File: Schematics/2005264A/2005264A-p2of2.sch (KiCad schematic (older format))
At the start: 65 parts, among them J3 ConnectorA1-300, J4 ConnectorA1-400, U202 D3NOR-+4SW-0VDCA-ABC-_F_, U203 D3NOR-FAP-0VDCA-expander-ABC-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, U204 D3NOR-+4SW-0VDCA-_C_-E_F, U205 D3NOR-+4SW-0VDCA-B_C-_F_, U206 D3NOR-+4SW-0VDCA-B_C-E_F, U207 D3NOR-+4SW-0VDCA-ABC-_F_, U208 D3NOR-FAP-0VDCA-expander-ABC-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, U209 D3NOR-+4SW-0VDCA-B_C-_F_, U210 D3NOR-+4SW-0VDCA-_C_-_F_, U211 D3NOR-+4SW-0VDCA-ABC-_F_, U212 D3NOR-FAP-0VDCA-expander-ABC-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, U213 D3NOR-+4SW-0VDCA-ACB-_F_, U214 D3NOR-+4SW-0VDCA-_C_-_F_, U215 D3NOR-+4SW-0VDCA-_C_-DEF, U216 D3NOR-FAP-0VDCA-expander-ABC-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, U217 D3NOR-+4SW-0VDCA-_C_-_F_, U218 D3NOR-+4SW-0VDCA-ACB-_F_, U219 D3NOR-+4SW-0VDCA-_C_-_F_, U220 D3NOR-+4SW-0VDCA-ABC-_F_, U221 D3NOR-+4SW-0VDCA-_C_-_F_, U222 D3NOR-FAP-0VDCA-expander-ABC-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, U223 D3NOR-+4SW-0VDCA-BAC-_F_, U224 D3NOR-+4SW-0VDCA-_C_-_F_, U225 D3NOR-+4SW-0VDCA-BAC-_F_, U226 D3NOR-+4SW-0VDCA-_C_-_F_, U227 D3NOR-FAP-0VDCA-expander-ABC-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, U228 D3NOR-+4SW-0VDCA-_C_-DEF, U229 D3NOR-+4SW-0VDCA-_C_-_F_, U230 D3NOR-+4SW-0VDCA-_C_-DEF, U231 D3NOR-+4SW-0VDCA-B_C-E_F, U232 D3NOR-+4SW-0VDCA-_C_-E_F, U233 D3NOR-+4SW-0VDCA-_C_-_F_, U234 D3NOR-+4SW-0VDCA-BAC-_F_, U235 D3NOR-+4SW-0VDCA-_C_-_F_, U236 D3NOR-+4SW-0VDCA-_C_-DFE, U237 D3NOR-+4SW-0VDCA-_C_-E_F, U238 D3NOR-FAP-0VDCA-expander-ABC-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, U239 D3NOR-FAP-0VDCA-expander-B_C-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, U240 D3NOR-+4SW-0VDCA-_C_-_F_, U241 D3NOR-+4SW-0VDCA-B_C-DFE, U242 D3NOR-+4SW-0VDCA-ACB-DFE, U243 D3NOR-FAP-0VDCA-expander-B_C-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, U244 D3NOR-+4SW-0VDCA-ABC-E_F, U245 D3NOR-+4SW-0VDCA-_C_-_F_, U246 D3NOR-FAP-0VDCA-expander-ABC-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, U247 D3NOR-+4SW-0VDCA-_C_-DFE, U248 D3NOR-+4SW-0VDCA-_C_-EDF, U249 D3NOR-FAP-0VDCA-expander-ABC-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, U250 D3NOR-+4SW-0VDCA-_C_-_F_, U251 D3NOR-+4SW-0VDCA-_C_-EDF, U252 D3NOR-+4SW-0VDCA-ACB-_F_, U253 D3NOR-+4SW-0VDCA-_C_-_F_, U254 D3NOR-FAP-0VDCA-expander-ABC-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, U255 D3NOR-+4SW-0VDCA-_C_-DEF, U256 D3NOR-+4SW-0VDCA-_C_-EDF, U257 D3NOR-+4SW-0VDCA-_C_-_F_, U258 D3NOR-FAP-0VDCA-expander-ABC-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, U259 D3NOR-+4SW-0VDCA-ACB-_F_, U260 D3NOR-+4SW-0VDCA-_C_-DFE, X1 ArrowTwiddle, X2 ArrowTwiddle, X3 ArrowTwiddle

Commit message: Added CAD files for drawing 2005264A.  Made several corrections to 2005264B that I found during the process.
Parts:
- J4: Caption 0VDCA -> WT/
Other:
- note added: "Notes from the Virtual AGC Project:\n1. This CAD drawing was adapted from the previously-transcribed original Apollo\n Program drawing 2005264B and checked vs the original drawing 2005264A (and\n 2005064F). It does not itself date from the Apollo period. — RSB 2018\n2. The original drawing displayed no reference designators for the components, so\n this CAD drawing also does not display any. For 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"
- note removed: "B REVISED PER TDRR 35326"
- note removed: "Notes from the Virtual AGC Project:\n1. This CAD drawing was manually transcribed from the original Apollo Program \n drawing 2005264B, but does not itself date from the Apollo period. — RSB 2018\n2. The original drawing displayed no reference designators for the components, so\n this CAD drawing also does not display any. For the purposes of ERC or netlist\n generation, NOR gates have reference 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"
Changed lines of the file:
@@
 Text Notes 38875 33400 0    140  ~ 28
 ____
-Wire Notes Line width 6 style solid
-	43500 1300 36461 1300
-Text Notes 36550 1250 0    160  ~ 32
-A      REVISED PER TDRR 30754
-Wire Notes Line width 6 style solid
-	43500 1625 36461 1625
-Wire Notes Line width 6 style solid
-	36461 975  36461 1625
-Wire Notes Line width 6 style solid
-	36839 975  36839 1625
-Wire Notes Line width 6 style solid
-	37350 975  37350 1625
-Wire Notes Line width 6 style solid
-	40831 975  40831 1625
-Wire Notes Line width 6 style solid
-	41331 975  41331 1625
-Wire Notes Line width 6 style solid
-	41831 975  41831 1625
-Wire Notes Line width 6 style solid
-	42480 975  42480 1625
-Text Notes 36525 1575 0    160  ~ 32
-B      REVISED PER TDRR 35326
 Text Notes 42425 33450 0    140  ~ 28
 2     2
@@
 F 2 "" H 24725 5300 140 0001 C CNN
 F 3 "" H 24725 5300 140 0001 C CNN
-F 4 "0VDCA" H 24550 5150 140 0000 C CNB "Caption"
+F 4 "WT/" H 24675 5175 140 0000 C CNB "Caption"
 	17   24725 4825
 	1    0    0    -1
@@
 F 2 "" H 9975 16175 140 0001 C CNN
 F 3 "" H 9975 16175 140 0001 C CNN
-F 4 "XB4/" H 9950 15375 140 0000 C CNB "Caption"
+F 4 "XB4/" H 9925 15375 140 0000 C CNB "Caption"
 	39   9975 15700
 	-1   0    0    1
@@
 $EndComp
 Text Notes 1175 33275 0    140  ~ 28
-Notes from the Virtual AGC Project:\n1. This CAD drawing was manually transcribed from the original Apollo Program \n   drawing 2005264B, but does not itself date from the Apollo period. — RSB 2018\n2. The original drawing displayed no reference designators for the components, so\n   this CAD drawing also does not display any.  For the purposes of ERC or netlist\n   generation, NOR gates have reference designators U2nn, where nn is the 2-digit\n   number shown on the NOR-gate symbol.  The oval pads numbered 301-371\n   comprise connector J3, while those numbered 401-471 comprise connector J4.\n   — RSB 2018\n3. All known revisions of this drawing incorrectly display the 2-digit location code of\n   NOR gate 42416 as "K".  On this CAD drawing, we have used location code "54",\n   so that the gate forms U254 (along with NOR gate 42412). — RSB 2018\n4. The originals of sheets 1 and 2 of drawing 2005264B used different \n   area-numbering systems.  Sheet 1 used border numbers 1-6 and border letters A-F,\n   while sheet 2 used numbers 1-8 and letters A-H.  The CAD schematic editor being\n   used does not provide the option of doing this, so the CAD drawing instead uses the\n   area-numbering system from sheet 1 for both sheets.\n5. The only change I have been able to find from drawing 2005264A to 2005264B is\n   that the caption of oval pad 417 has changed from "WT/" to "0VDCA". — RSB 2018
+Notes from the Virtual AGC Project:\n1. This CAD drawing was adapted from the previously-transcribed original Apollo\n   Program drawing 2005264B and checked vs the original drawing 2005264A (and\n   2005064F).  It does not itself date from the Apollo period.  — RSB 2018\n2. The original drawing displayed no reference designators for the components, so\n   this CAD drawing also does not display any.  For the purposes of ERC or netlist\n   generation, NOR gates have reference designators U2nn, where nn is the 2-digit\n   number shown on the NOR-gate symbol.  The oval pads numbered 301-371\n   comprise connector J3, while those numbered 401-471 comprise connector J4.\n   — RSB 2018\n3. All known revisions of this drawing incorrectly display the 2-digit location code of\n   NOR gate 42416 as "K".  On this CAD drawing, we have used location code "54",\n   so that the gate forms U254 (along with NOR gate 42412). — RSB 2018\n4. The originals of sheets 1 and 2 of drawing 2005264A used different \n   area-numbering systems.  Sheet 1 used border numbers 1-6 and border letters A-F,\n   while sheet 2 used numbers 1-8 and letters A-H.  The CAD schematic editor being\n   used does not provide the option of doing this, so the CAD drawing instead uses the\n   area-numbering system from sheet 1 for both sheets.
 Wire Wire Line
 	8125 4525 8350 4525
@@
 Wire Wire Line
 	16725 16125 17000 16125
+Wire Notes Line width 6 style solid
+	43500 1300 36461 1300
+Text Notes 36550 1250 0    160  ~ 32
+A      REVISED PER TDRR 30754
+Wire Notes Line width 6 style solid
+	36461 975  36461 1300
+Wire Notes Line width 6 style solid
+	36839 975  36839 1300
+Wire Notes Line width 6 style solid
+	37350 975  37350 1300
+Wire Notes Line width 6 style solid
+	40831 975  40831 1300
+Wire Notes Line width 6 style solid
+	41331 975  41331 1300
+Wire Notes Line width 6 style solid
+	41831 975  41831 1300
+Wire Notes Line width 6 style solid
+	42480 975  42480 1300
 $Bitmap
-Pos 925  29000
+Pos 925  29225
 Scale 1.000000
 Data

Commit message: Finished up CAD for 2005264-, and made a correction to 2005264A & B based on the proofing for it.
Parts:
- J3: Caption XB73 -> XB7E
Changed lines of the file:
@@
 EESchema Schematic File Version 4
-LIBS:module-cache
 EELAYER 26 0
 EELAYER END
 $Descr E 44000 34000
 encoding utf-8
-Sheet 3 3
+Sheet 1 1
 Title ""
 Date ""
@@
 F 2 "" H 11425 27300 140 0001 C CNN
 F 3 "" H 11425 27300 140 0001 C CNN
-F 4 "XB73" H 11450 26475 140 0000 C CNB "Caption"
+F 4 "XB7E" H 11450 26475 140 0000 C CNB "Caption"
 	25   11425 26825
 	-1   0    0    1

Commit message: Cross-checked/corrected module A14's 2005264A and 2005264B drawings vs pin database.  Predecessor drawings (2005264- etc.) not yet corrected.
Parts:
- J3, J4: Caption (none) -> 0VDCA
- J3: Caption 208 -> S08
- J3, J4: Caption (none) -> +4SW
- J4: Caption WSC6/ -> WSCG/
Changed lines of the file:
@@
 EESchema Schematic File Version 4
+LIBS:module-cache
 EELAYER 26 0
 EELAYER END
 $Descr E 44000 34000
 encoding utf-8
-Sheet 1 1
+Sheet 3 3
 Title ""
 Date ""
@@
 F 2 "" H 31650 5275 140 0001 C CNN
 F 3 "" H 31650 5275 140 0001 C CNN
-F 4 "WSC6/" H 31675 4450 140 0000 C CNB "Caption"
+F 4 "WSCG/" H 31675 4450 140 0000 C CNB "Caption"
 	11   31650 4800
 	-1   0    0    1
@@
 F 2 "" H 40350 27475 140 0001 C CNN
 F 3 "" H 40350 27475 140 0001 C CNN
-F 4 "" H 40350 27300 140 0000 C CNB "Caption"
+F 4 "0VDCA" H 40350 27300 140 0001 C CNB "Caption"
 	12   40350 27000
 	1    0    0    -1
@@
 F 2 "" H 36475 28500 140 0001 C CNN
 F 3 "" H 36475 28500 140 0001 C CNN
-F 4 "" H 36475 28325 140 0000 C CNB "Caption"
+F 4 "0VDCA" H 36475 28325 140 0001 C CNB "Caption"
 	60   36475 28025
 	1    0    0    -1
@@
 F 2 "" H 40350 28475 140 0001 C CNN
 F 3 "" H 40350 28475 140 0001 C CNN
-F 4 "" H 40350 28300 140 0000 C CNB "Caption"
+F 4 "0VDCA" H 40350 28300 140 0001 C CNB "Caption"
 	60   40350 28000
 	1    0    0    -1
@@
 F 2 "" H 40350 27975 140 0001 C CNN
 F 3 "" H 40350 27975 140 0001 C CNN
-F 4 "" H 40350 27800 140 0000 C CNB "Caption"
+F 4 "0VDCA" H 40350 27800 140 0001 C CNB "Caption"
 	36   40350 27500
 	1    0    0    -1
@@
 F 2 "" H 40350 29800 140 0001 C CNN
 F 3 "" H 40350 29800 140 0001 C CNN
-F 4 "" H 40350 29625 140 0000 C CNB "Caption"
+F 4 "+4SW" H 40350 29625 140 0001 C CNB "Caption"
 	48   40350 29325
 	1    0    0    -1
@@
 F 2 "" H 36475 29325 140 0001 C CNN
 F 3 "" H 36475 29325 140 0001 C CNN
-F 4 "" H 36475 29150 140 0000 C CNB "Caption"
+F 4 "+4SW" H 36475 29150 140 0001 C CNB "Caption"
 	24   36475 28850
 	1    0    0    -1
@@
 F 2 "" H 40325 29300 140 0001 C CNN
 F 3 "" H 40325 29300 140 0001 C CNN
-F 4 "" H 40325 29125 140 0000 C CNB "Caption"
+F 4 "+4SW" H 40325 29125 140 0001 C CNB "Caption"
 	24   40325 28825
 	1    0    0    -1
@@
 F 2 "" H 12175 6500 140 0001 C CNN
 F 3 "" H 12175 6500 140 0001 C CNN
-F 4 "208" H 12175 6325 140 0000 C CNB "Caption"
+F 4 "S08" H 12175 6325 140 0000 C CNB "Caption"
 	17   12175 6025
 	1    0    0    -1
@@
 F 2 "" H 36475 27500 140 0001 C CNN
 F 3 "" H 36475 27500 140 0001 C CNN
-F 4 "" H 36475 27325 140 0000 C CNB "Caption"
+F 4 "0VDCA" H 36475 27325 140 0001 C CNB "Caption"
 	12   36475 27025
 	1    0    0    -1

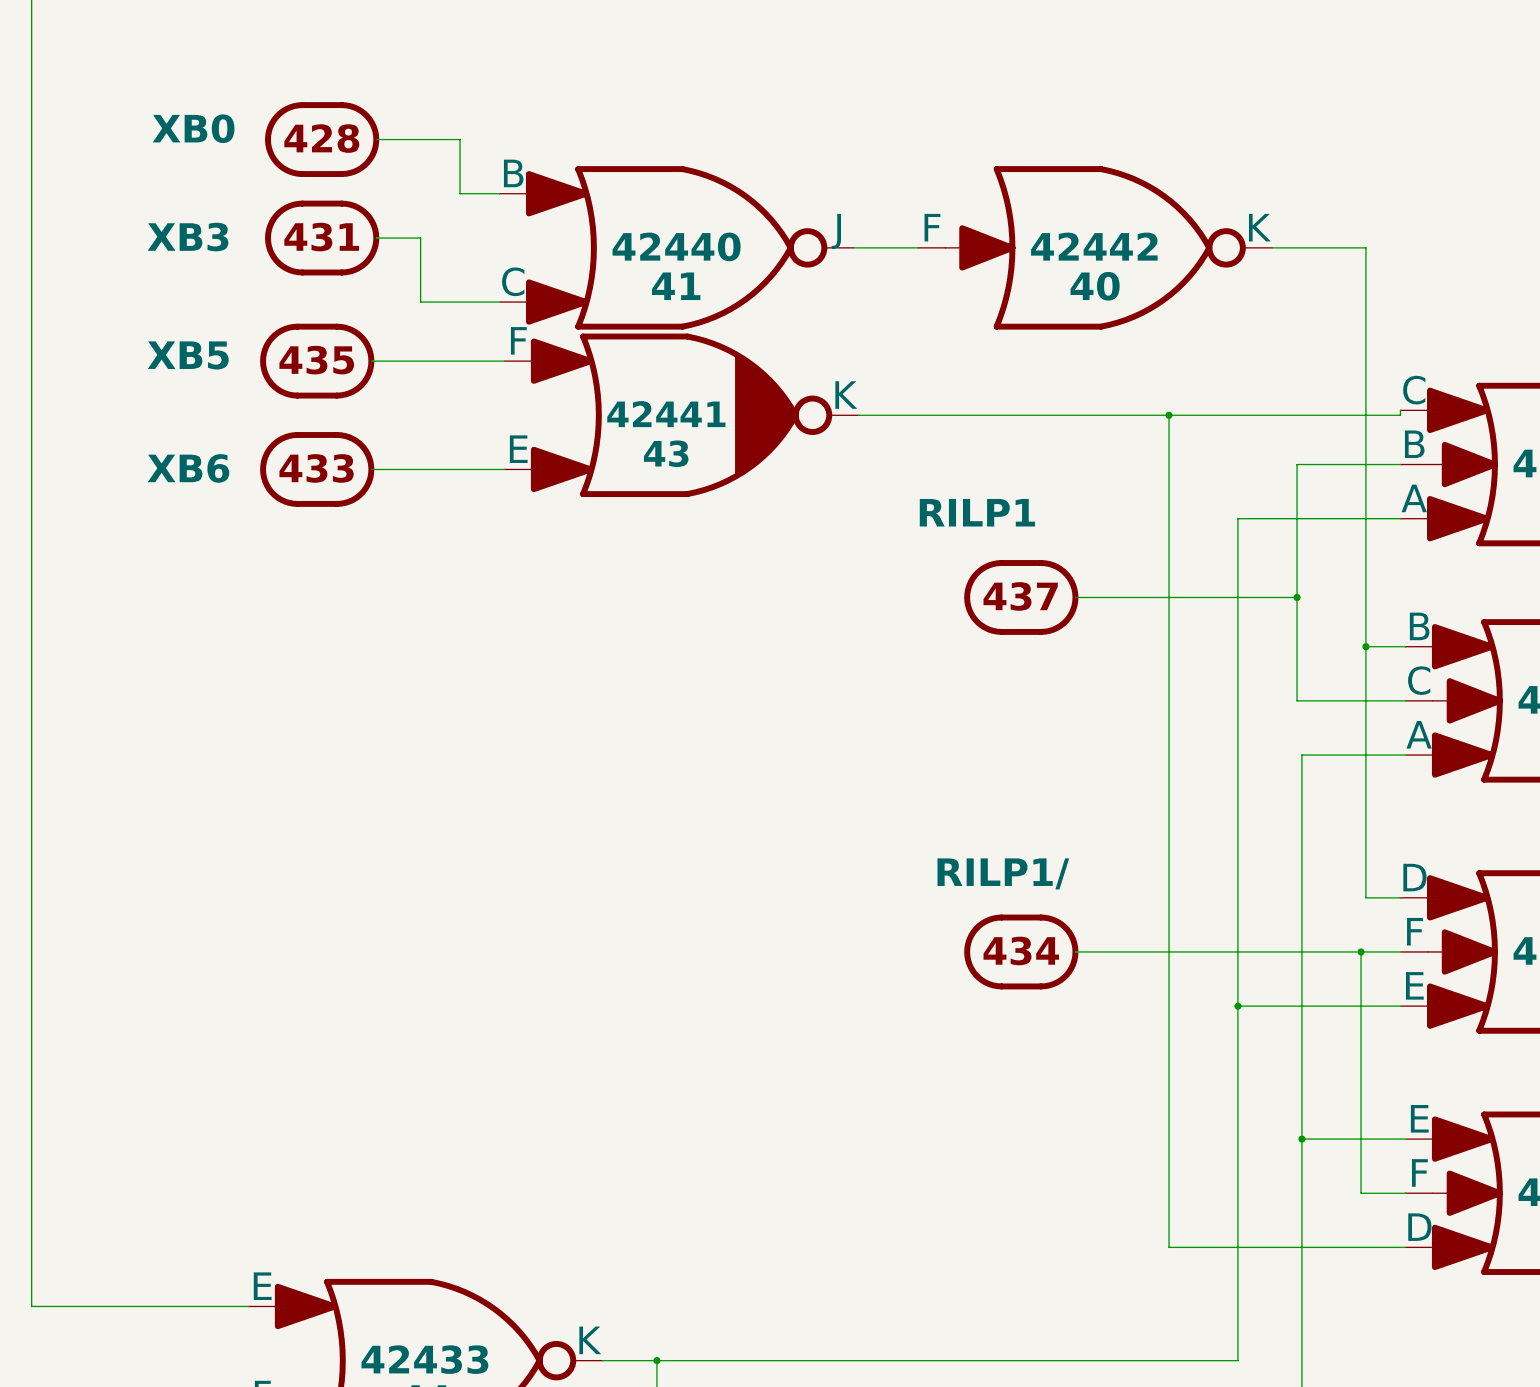
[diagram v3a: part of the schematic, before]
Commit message: Corrected a wiring bug.
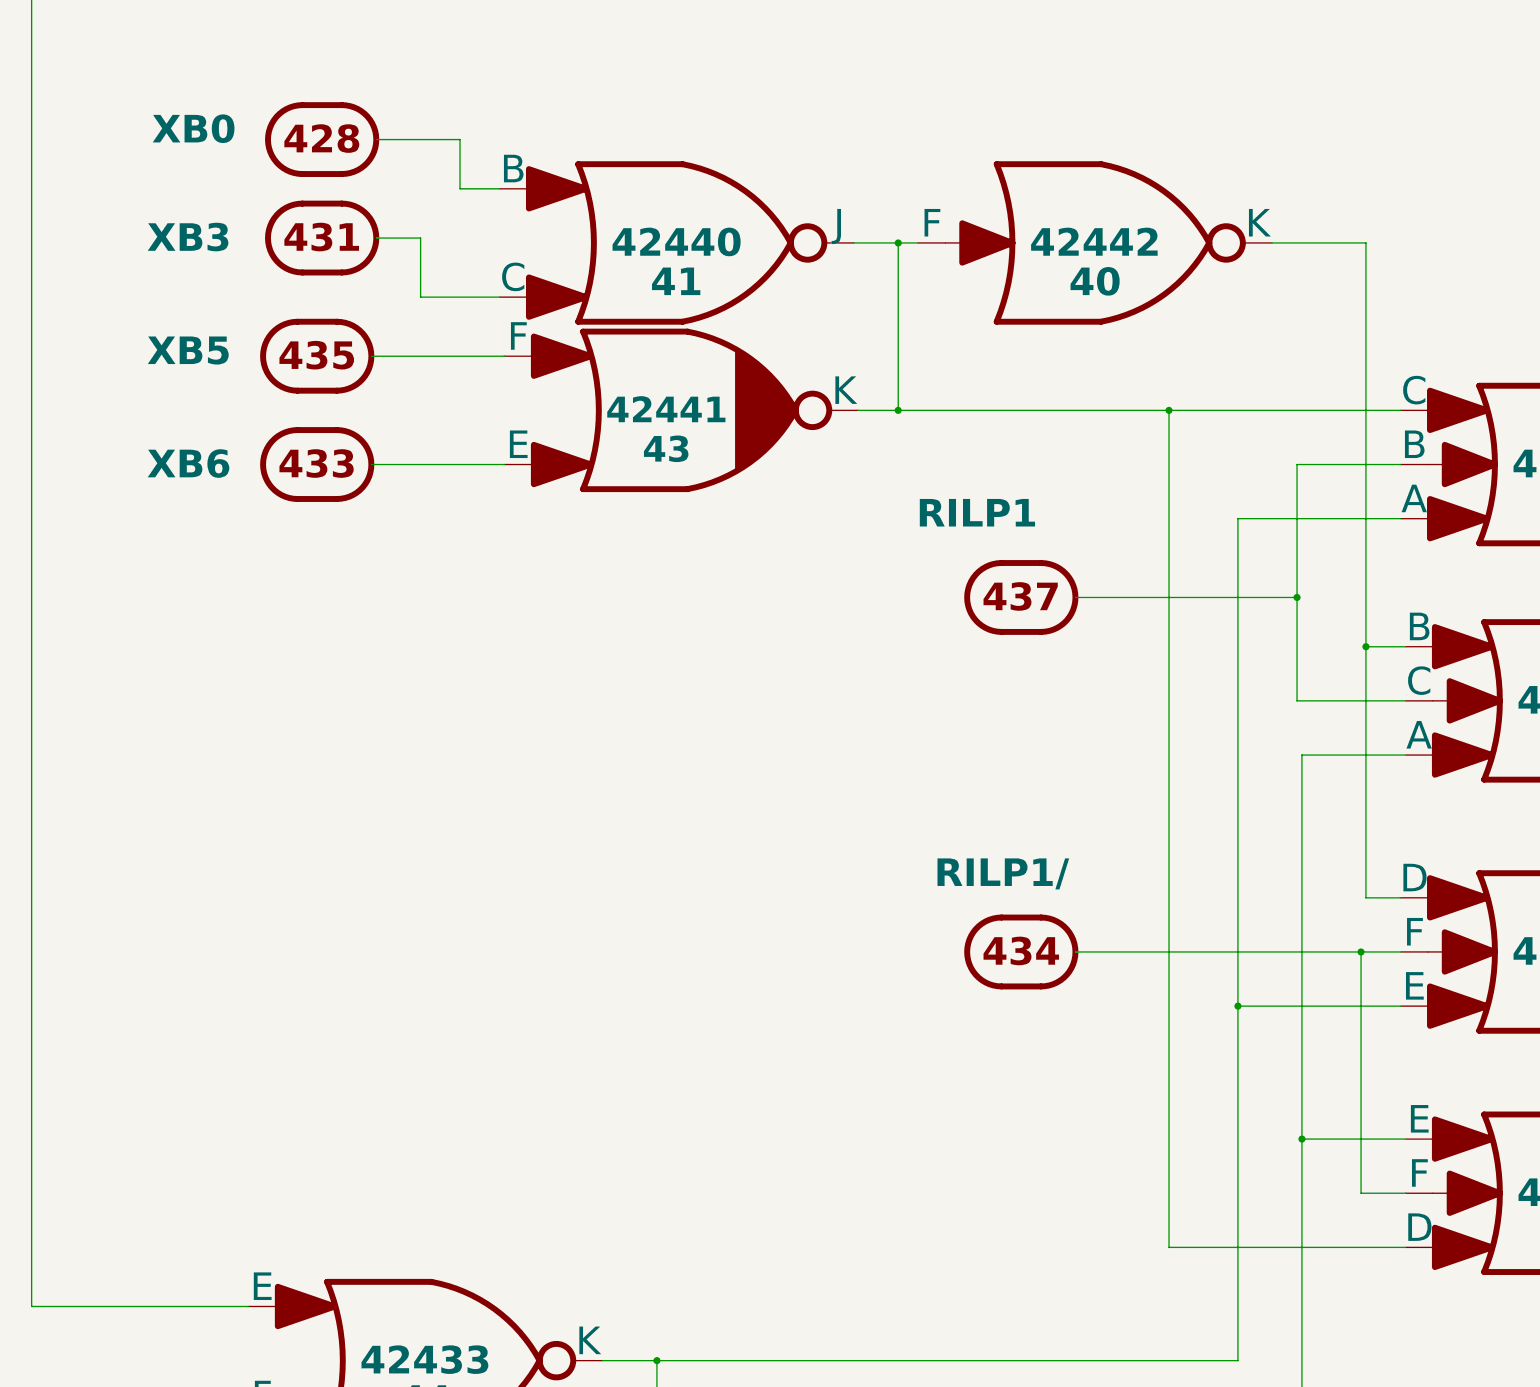
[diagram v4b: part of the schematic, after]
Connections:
- net at U241.6 (D), U243.9 (K), U244.2 (C): now also U240.8 (F), U241.1 (J)
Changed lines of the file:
@@
 EESchema Schematic File Version 4
 LIBS:module-cache
-EELAYER 26 0
+EELAYER 29 0
 EELAYER END
 $Descr E 44000 34000
@@
 L D3NOR-FAP-0VDCA-expander:D3NOR-FAP-0VDCA-expander-B_C-E_F U243
 U 2 1 5F3BC912
-P 35000 12275
-F 0 "U243" H 35000 12600 140 0001 C CNB
-F 1 "D3NOR-FAP-0VDCA-expander-B_C-E_F" H 35000 12700 140 0001 C CNN
-F 2 "" H 35000 12750 140 0001 C CNN
-F 3 "" H 35000 12750 140 0001 C CNN
-F 4 "42441" H 34925 12275 130 0000 C CNB "Location"
-F 5 "43" H 34925 12475 130 0000 C CNB "Location2"
-	2    35000 12275
+P 35000 12250
+F 0 "U243" H 35000 12575 140 0001 C CNB
+F 1 "D3NOR-FAP-0VDCA-expander-B_C-E_F" H 35000 12675 140 0001 C CNN
+F 2 "" H 35000 12725 140 0001 C CNN
+F 3 "" H 35000 12725 140 0001 C CNN
+F 4 "42441" H 34925 12250 130 0000 C CNB "Location"
+F 5 "43" H 34925 12450 130 0000 C CNB "Location2"
+	2    35000 12250
 	1    0    0    1
 $EndComp
@@
 L AGC_DSKY:ConnectorA1-400 J4
 U 35 1 5F3BC9D5
-P 33150 12000
-F 0 "J4" H 33150 12325 140 0001 C CNN
-F 1 "ConnectorA1-400" H 33150 12425 140 0001 C CNN
-F 2 "" H 33150 12475 140 0001 C CNN
-F 3 "" H 33150 12475 140 0001 C CNN
-F 4 "XB5" H 32500 12025 140 0000 C CNB "Caption"
-	35   33150 12000
+P 33150 11975
+F 0 "J4" H 33150 12300 140 0001 C CNN
+F 1 "ConnectorA1-400" H 33150 12400 140 0001 C CNN
+F 2 "" H 33150 12450 140 0001 C CNN
+F 3 "" H 33150 12450 140 0001 C CNN
+F 4 "XB5" H 32500 12000 140 0000 C CNB "Caption"
+	35   33150 11975
 	1    0    0    -1
 $EndComp
@@
 L AGC_DSKY:ConnectorA1-400 J4
 U 33 1 5F3BC9F8
-P 33150 12550
-F 0 "J4" H 33150 12875 140 0001 C CNN
-F 1 "ConnectorA1-400" H 33150 12975 140 0001 C CNN
-F 2 "" H 33150 13025 140 0001 C CNN
-F 3 "" H 33150 13025 140 0001 C CNN
-F 4 "XB6" H 32500 12550 140 0000 C CNB "Caption"
-	33   33150 12550
+P 33150 12525
+F 0 "J4" H 33150 12850 140 0001 C CNN
+F 1 "ConnectorA1-400" H 33150 12950 140 0001 C CNN
+F 2 "" H 33150 13000 140 0001 C CNN
+F 3 "" H 33150 13000 140 0001 C CNN
+F 4 "XB6" H 32500 12525 140 0000 C CNB "Caption"
+	33   33150 12525
 	1    0    0    -1
 $EndComp
@@
 L D3NOR-+4SW-0VDCA:D3NOR-+4SW-0VDCA-B_C-DFE U241
 U 1 1 5F3BC98E
-P 34975 11425
-F 0 "U241" H 34975 11750 140 0001 C CNB
-F 1 "D3NOR-+4SW-0VDCA-B_C-DFE" H 34975 11850 140 0001 C CNN
-F 2 "" H 34975 11900 140 0001 C CNN
-F 3 "" H 34975 11900 140 0001 C CNN
-F 4 "42440" H 34975 11425 140 0000 C CNB "Location"
-F 5 "41" H 34975 11225 140 0000 C CNB "Location2"
-	1    34975 11425
+P 34975 11400
+F 0 "U241" H 34975 11725 140 0001 C CNB
+F 1 "D3NOR-+4SW-0VDCA-B_C-DFE" H 34975 11825 140 0001 C CNN
+F 2 "" H 34975 11875 140 0001 C CNN
+F 3 "" H 34975 11875 140 0001 C CNN
+F 4 "42440" H 34975 11400 140 0000 C CNB "Location"
+F 5 "41" H 34975 11200 140 0000 C CNB "Location2"
+	1    34975 11400
 	1    0    0    -1
 $EndComp
@@
 L D3NOR-+4SW-0VDCA:D3NOR-+4SW-0VDCA-_C_-_F_ U240
 U 2 1 5F3BC98B
-P 37100 11425
-F 0 "U240" H 37100 11750 140 0001 C CNB
-F 1 "D3NOR-+4SW-0VDCA-_C_-_F_" H 37100 11850 140 0001 C CNN
-F 2 "" H 37100 11900 140 0001 C CNN
-F 3 "" H 37100 11900 140 0001 C CNN
-F 4 "42442" H 37100 11425 140 0000 C CNB "Location"
-F 5 "40" H 37100 11625 140 0000 C CNB "Location2"
-	2    37100 11425
+P 37100 11400
+F 0 "U240" H 37100 11725 140 0001 C CNB
+F 1 "D3NOR-+4SW-0VDCA-_C_-_F_" H 37100 11825 140 0001 C CNN
+F 2 "" H 37100 11875 140 0001 C CNN
+F 3 "" H 37100 11875 140 0001 C CNN
+F 4 "42442" H 37100 11400 140 0000 C CNB "Location"
+F 5 "40" H 37100 11600 140 0000 C CNB "Location2"
+	2    37100 11400
 	1    0    0    1
 $EndComp
@@
 	34650 18175 34875 18175
 Wire Wire Line
-	35875 11425 36200 11425
+	35875 11400 36100 11400
 Wire Wire Line
-	35900 12275 37475 12275
-Wire Wire Line
-	38650 12275 38650 12250
+	35900 12250 36100 12250
 Wire Wire Line
 	33450 10875 33875 10875
 Wire Wire Line
-	33875 10875 33875 11150
+	33875 10875 33875 11125
 Wire Wire Line
-	33875 11150 34075 11150
+	33875 11125 34075 11125
 Wire Wire Line
 	33450 11375 33675 11375
 Wire Wire Line
-	33675 11375 33675 11700
+	33675 11375 33675 11675
 Wire Wire Line
-	33675 11700 34075 11700
+	33675 11675 34075 11675
 Wire Wire Line
-	34100 12000 33425 12000
+	34100 11975 33425 11975
 Wire Wire Line
-	34100 12550 33425 12550
+	34100 12525 33425 12525
 Wire Wire Line
-	38000 11425 38475 11425
+	38000 11400 38475 11400
 Wire Wire Line
-	38475 11425 38475 13450
+	38475 11400 38475 13450
 Wire Wire Line
 	38475 14725 38650 14725
@@
 	38675 16500 37475 16500
 Wire Wire Line
-	37475 16500 37475 12275
-Connection ~ 37475 12275
+	37475 16500 37475 12250
+Connection ~ 37475 12250
 Wire Wire Line
-	37475 12275 38650 12275
+	37475 12250 38650 12250
 Wire Wire Line
 	40450 12525 40875 12525
@@
 EndData
 $EndBitmap
+Wire Wire Line
+	36100 11400 36100 12250
+Connection ~ 36100 11400
+Wire Wire Line
+	36100 11400 36200 11400
+Connection ~ 36100 12250
+Wire Wire Line
+	36100 12250 37475 12250
 $EndSCHEMATC
